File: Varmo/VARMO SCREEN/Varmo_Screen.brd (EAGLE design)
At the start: 40 x 98 mm, 36 parts, among them T1 MMBT2222AL, U1 LT1813, U2 PCA9670D, U5 90814-0210

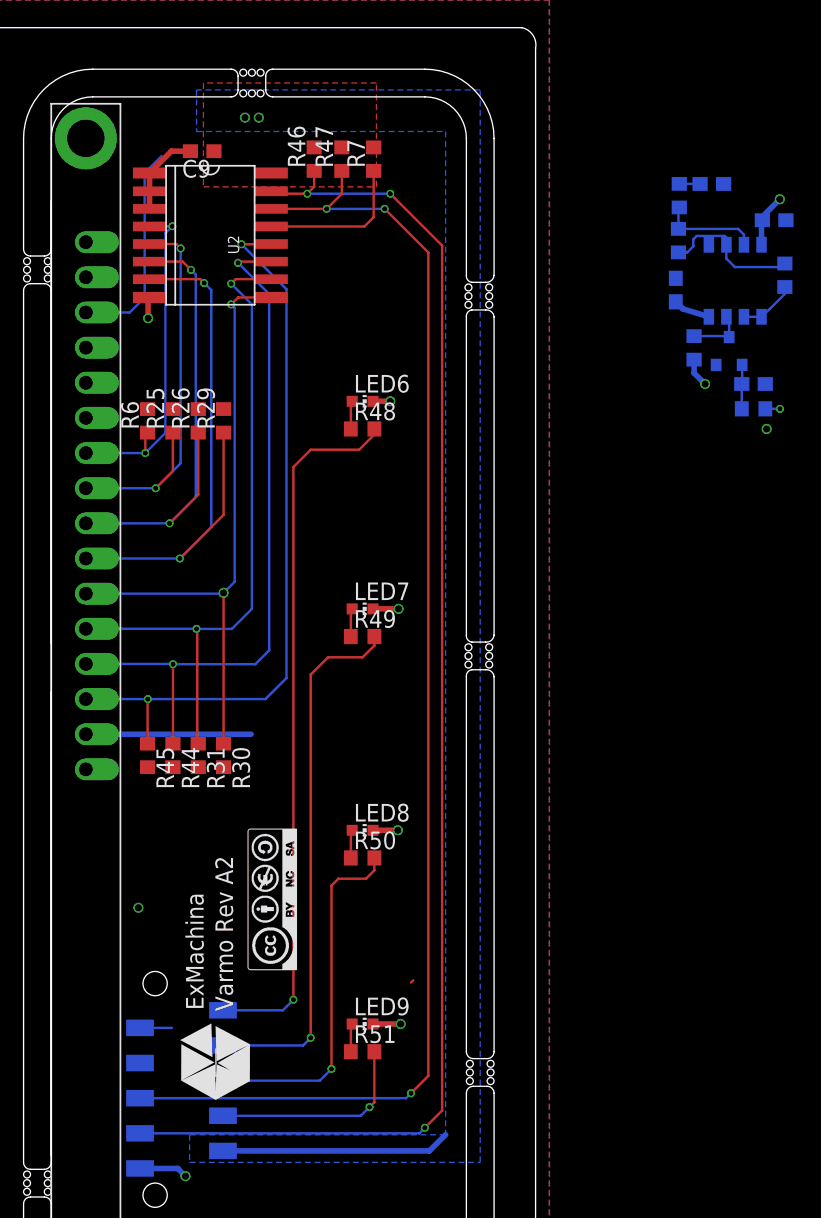
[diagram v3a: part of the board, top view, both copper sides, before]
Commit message: Add TLP0401A to the schematic and route the board
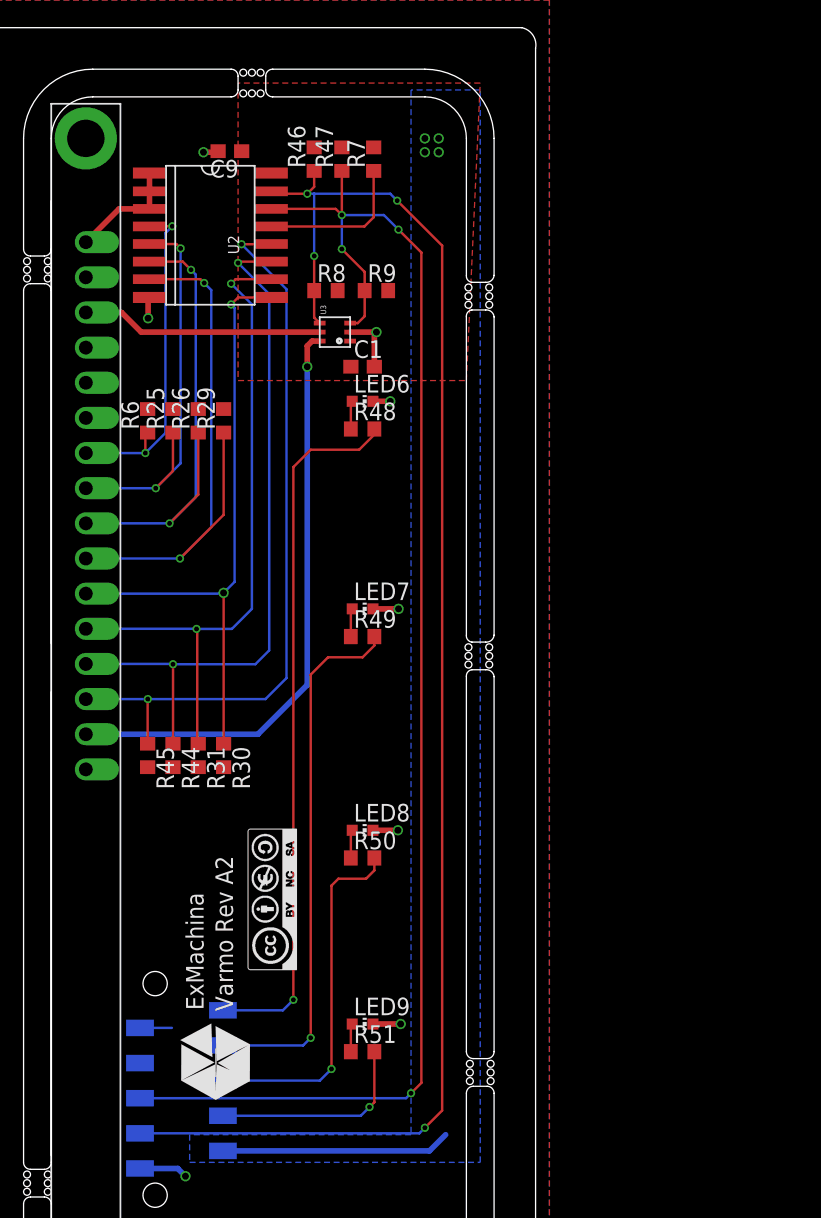
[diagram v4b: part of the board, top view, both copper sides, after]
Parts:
- removed C10, C4, C6: 0.1uF, rcl:C0603
- removed C5: 4.7uF, rcl:C0603
- removed R1: 100R, rcl:R0603
- removed R2, R3, R4: 1k, rcl:R0603
- removed R5: 10k, rcl:R0603
- removed T1: MMBT2222AL, transistor:SOT−23
- removed U1: LT1813, lineartechnology:S8
- added C1: 0.1uF, rcl:C0603
- added R8, R9: 4.7k, rcl:R0603
- added U3: TPL0401A, ti:SC-70-DCK
- moved C9 2.00 mm to (10.9, 82.1)
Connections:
- removed net N$14: R3.1, R4.2, U1.6
- removed net N$17: R4.1, R5.2, U1.7
- removed net N$2: C4.1, R1.2, T1.1
- removed net N$3: R2.1, T1.3, U1.3
- removed net N$5: R3.2, U1.1, U1.2
- net +3V3: now also C1.1, R8.2, R9.2, U3.1
- net +5V/1: no longer C6.1, R2.2, U1.8
- net GND1: now also C1.2, U3.2; no longer C10.2, C4.2, C5.2, C6.2, T1.2, U1.5
- net PWM_CONTRASTE: no longer R1.1
- net SCL: now also R9.1, U3.3
- net SDA: now also R8.1, U3.4
- net VEE: now also U3.6; no longer C10.1, U1.4
- net VO: now also U3.5; no longer C5.1, R5.1
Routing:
- net VEE: track 14.6 -> 43.0 mm, vias 0 -> 1
- net N$14: track 10.4 -> 0.00 mm
- net SDA: track 100.9 -> 110.4 mm, vias 3 -> 4
- net SCL: track 96.9 -> 105.4 mm, vias 3 -> 4
- net GND1: track 15.0 -> 22.4 mm
- net N$17: track 7.21 -> 0.00 mm
- net +5V/1: track 9.44 -> 3.52 mm, vias 3 -> 1
- net N$3: track 4.83 -> 0.00 mm
- net N$5: track 4.13 -> 0.00 mm
- net N$2: track 3.19 -> 0.00 mm
- net PWM_CONTRASTE: track 3.59 -> 2.30 mm, vias 1 -> 0
- net VO: track 16.9 -> 17.5 mm
- net +3V3: vias 2 -> 4

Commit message: Deleted wrong trace
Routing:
- net +3V3: track 16.6 -> 0.00 mm
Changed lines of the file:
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@@
 <contactref element="C9" pad="1"/>
 <contactref element="U5" pad="2"/>
-<wire x1="10.4094" y1="9.83" x2="25.33" y2="9.83" width="0.4064" layer="16"/>
-<wire x1="25.33" y1="9.83" x2="26.5" y2="11" width="0.4064" layer="16"/>
 <polygon width="0.4064" layer="16">
 <vertex x="24" y="86.5"/>

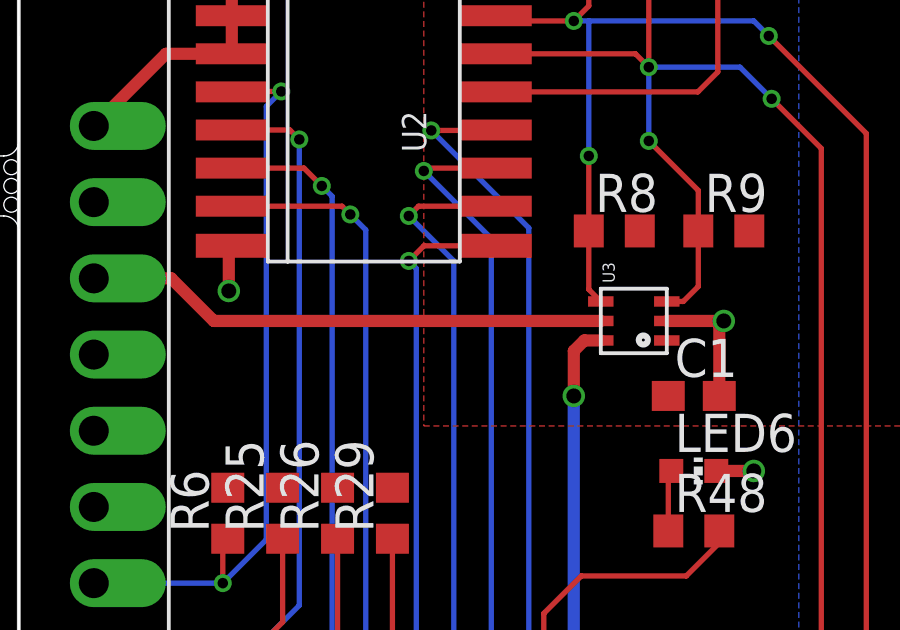
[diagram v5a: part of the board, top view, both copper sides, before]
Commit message: Add manuel potentiometer
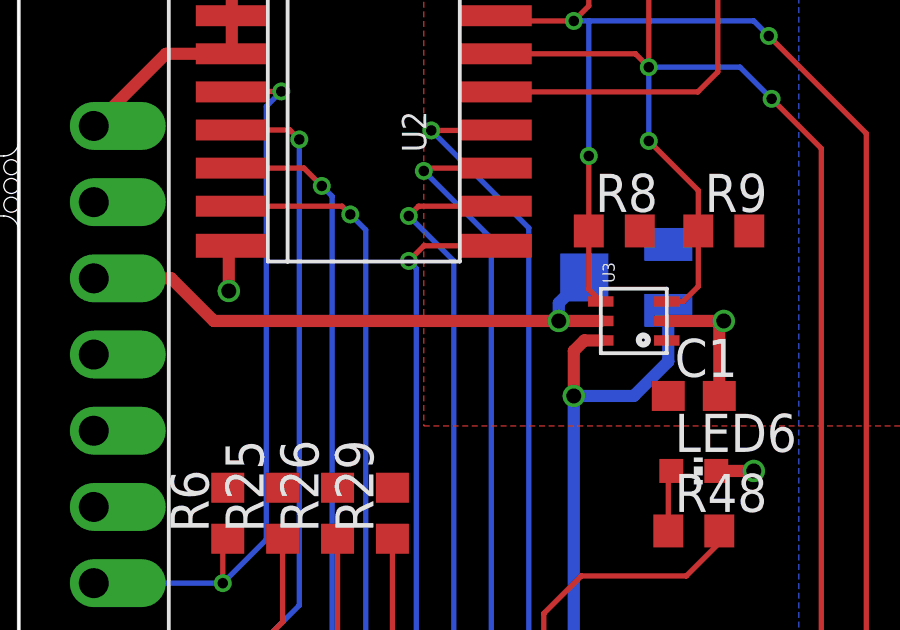
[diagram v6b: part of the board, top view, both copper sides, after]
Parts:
- added R1: 3313J-1-103E, pot:3313J
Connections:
- net GND1: now also R1.3
- net VEE: now also R1.1
- net VO: now also R1.2
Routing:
- net VEE: track 43.0 -> 48.3 mm
- net VO: track 17.5 -> 19.3 mm, vias 0 -> 1
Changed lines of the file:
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@@
 <element name="R8" library="rcl" package="R0603" value="4.7k" x="17.85" y="72"/>
 <element name="R9" library="rcl" package="R0603" value="4.7k" x="21.5" y="72"/>
+<element name="R1" library="pot" package="3313J" value="3313J-1-103E" x="18.25" y="70.45" rot="MR270"/>
 </elements>
 <signals>
@@
 <wire x1="9.985" y1="82" x2="9" y2="82" width="0.4064" layer="1"/>
 <via x="9" y="82" extent="1-16" drill="0.5"/>
+<contactref element="R1" pad="3"/>
 </signal>
 <signal name="+5V/1">
@@
 <contactref element="LCD1" pad="3"/>
 <contactref element="U3" pad="5"/>
-<wire x1="17.4" y1="69" x2="4.5" y2="69" width="0.4064" layer="1"/>
+<wire x1="17.4" y1="69" x2="16" y2="69" width="0.4064" layer="1"/>
+<wire x1="16" y1="69" x2="4.5" y2="69" width="0.4064" layer="1"/>
 <wire x1="4.5" y1="69" x2="3.08" y2="70.42" width="0.4064" layer="1"/>
 <wire x1="3.08" y1="70.42" x2="0.5" y2="70.42" width="0.4064" layer="1"/>
+<contactref element="R1" pad="2"/>
+<via x="16" y="69" extent="1-16" drill="0.5"/>
+<wire x1="16.85" y1="70.45" x2="16" y2="69.6" width="0.4064" layer="16"/>
+<wire x1="16" y1="69.6" x2="16" y2="69" width="0.4064" layer="16"/>
 </signal>
 <signal name="VEE">
@@
 <wire x1="16.5" y1="68" x2="16.5" y2="66.5" width="0.4064" layer="1"/>
 <via x="16.5" y="66.5" extent="1-16" drill="0.5"/>
+<contactref element="R1" pad="1"/>
+<wire x1="19.65" y1="69.35" x2="19.65" y2="67.65" width="0.4064" layer="16"/>
+<wire x1="19.65" y1="67.65" x2="18.5" y2="66.5" width="0.4064" layer="16"/>
+<wire x1="18.5" y1="66.5" x2="16.5" y2="66.5" width="0.4064" layer="16"/>
 </signal>
 <signal name="PWM_CONTRASTE">

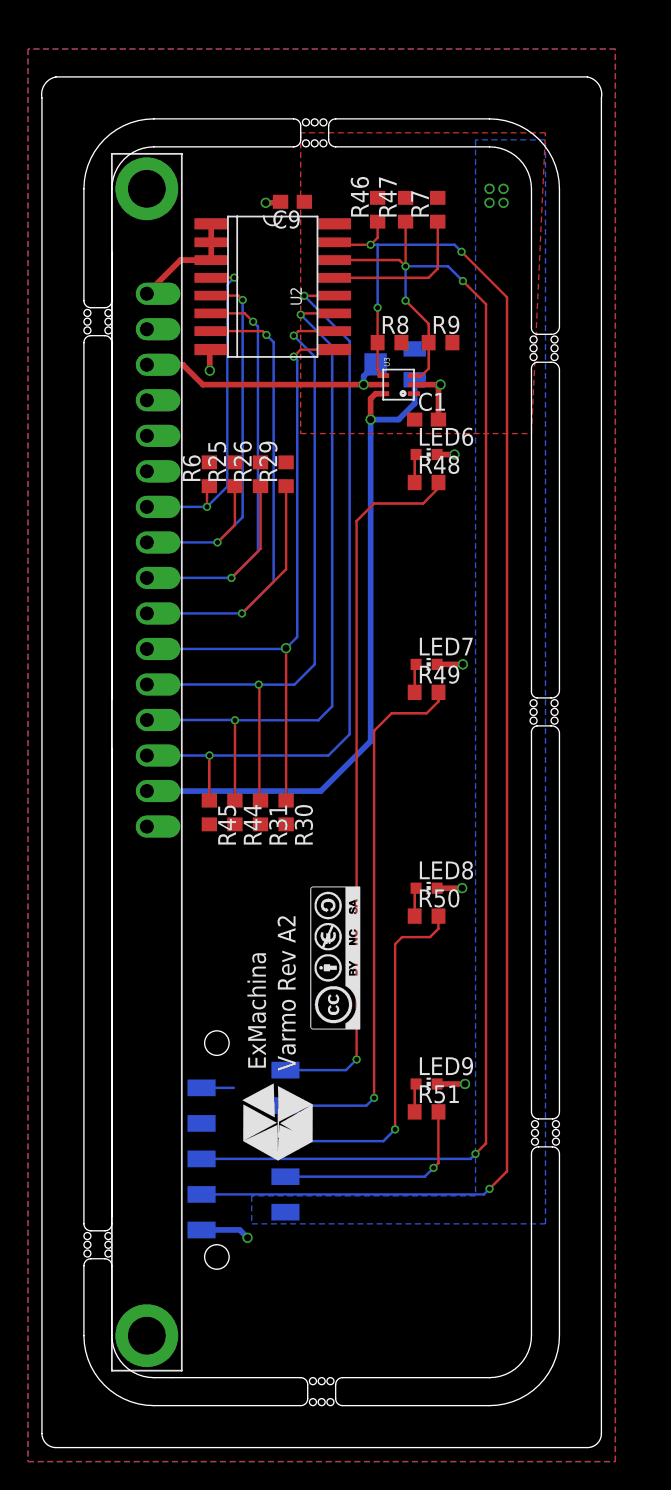
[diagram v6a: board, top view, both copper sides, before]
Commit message: Deleted the edge of the board and generate the gerber files
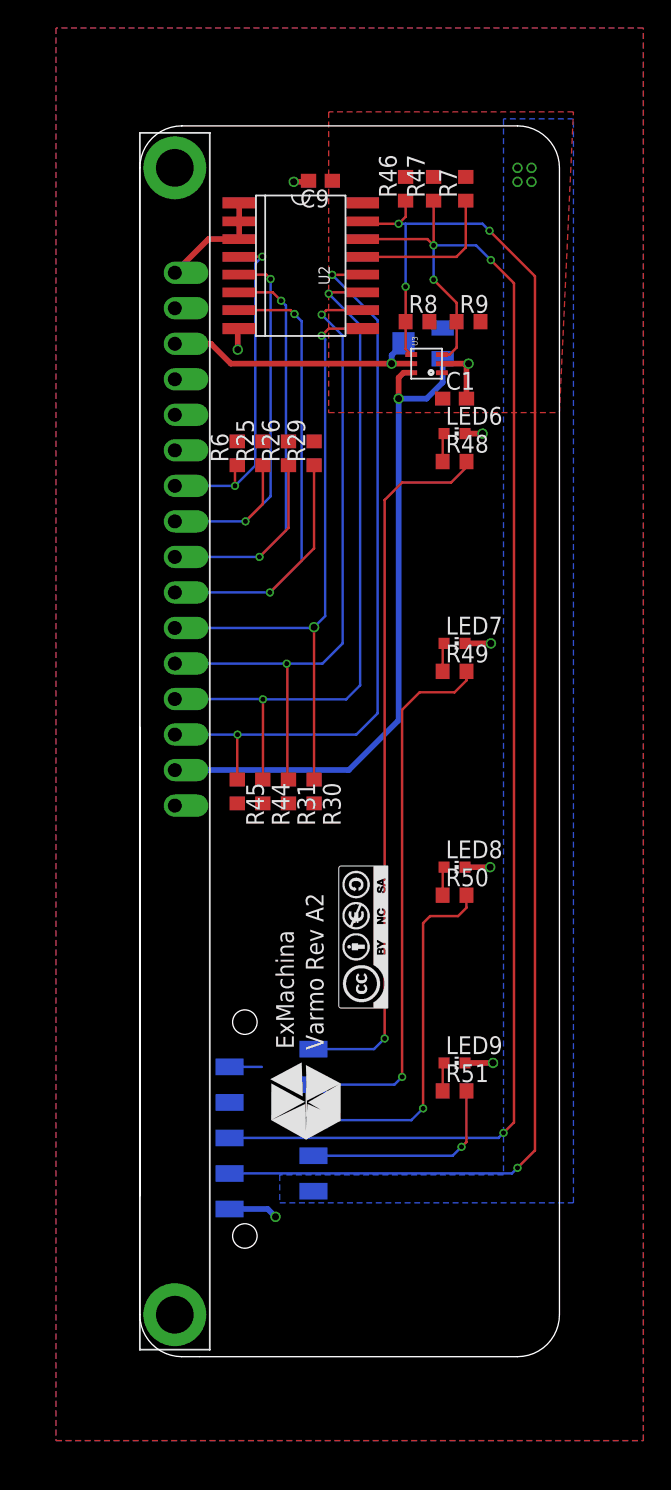
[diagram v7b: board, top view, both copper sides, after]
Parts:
- moved C1 2.50 mm to (22.5, 68.0)
- moved C9 2.50 mm to (12.9, 83.6)
- moved LCD1 2.50 mm to (2.50, 43.5)
- moved LED6 2.50 mm to (22.5, 65.5)
- moved LED7 2.50 mm to (22.5, 50.5)
- moved LED8 2.50 mm to (22.5, 34.5)
- moved LED9 2.50 mm to (22.5, 20.5)
- moved R1 2.50 mm to (20.2, 72.0)
- moved R25 2.50 mm to (8.79, 64.1)
- moved R26 2.50 mm to (10.6, 64.1)
- moved R29 2.50 mm to (12.5, 64.1)
- moved R30 2.50 mm to (12.5, 39.9)
- moved R31 2.50 mm to (10.6, 39.9)
- moved R44 2.50 mm to (8.79, 39.9)
- moved R45 2.50 mm to (6.96, 39.9)
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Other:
- board size 40 x 98 mm -> 30 x 88 mm
